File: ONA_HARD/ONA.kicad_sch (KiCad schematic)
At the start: 48 parts, among them J1 USB_C_Receptacle_USB2.0_16P, U1 ESP32-S3-WROOM-1U, U2 PC817, U3 LM2596S-5, U4 AMS1117-3.3, U6 MAX3485, U7 MAX3485, U8 MAX3485

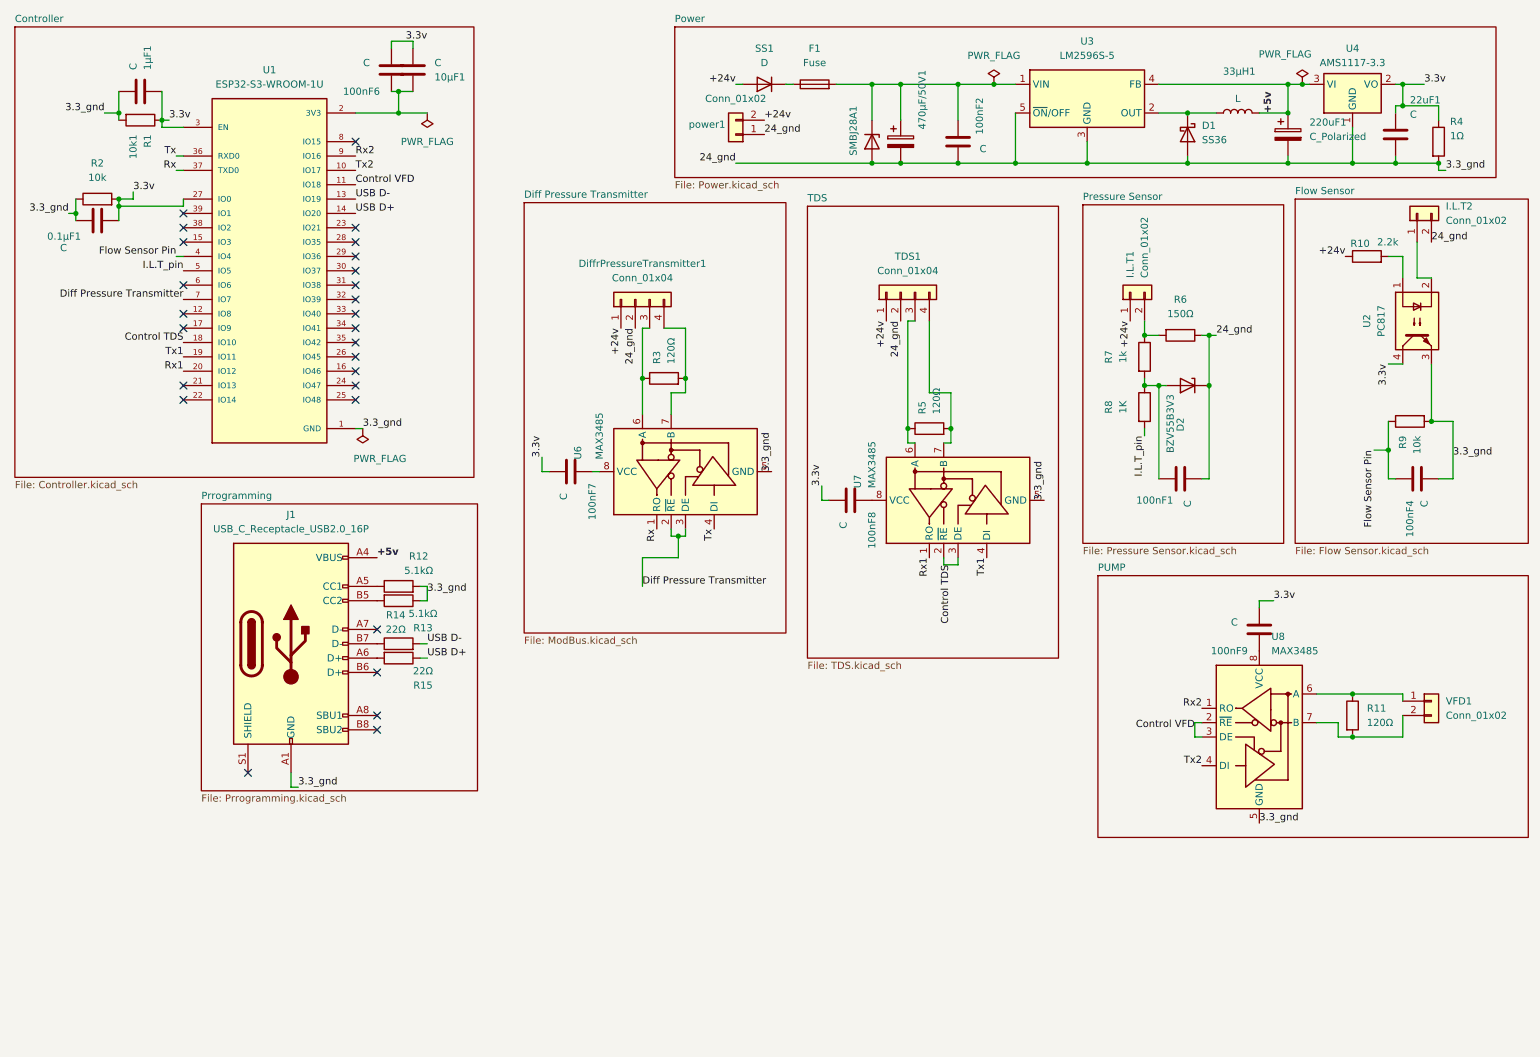
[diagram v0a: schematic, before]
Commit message: chore: remove .history folders and add to gitignore
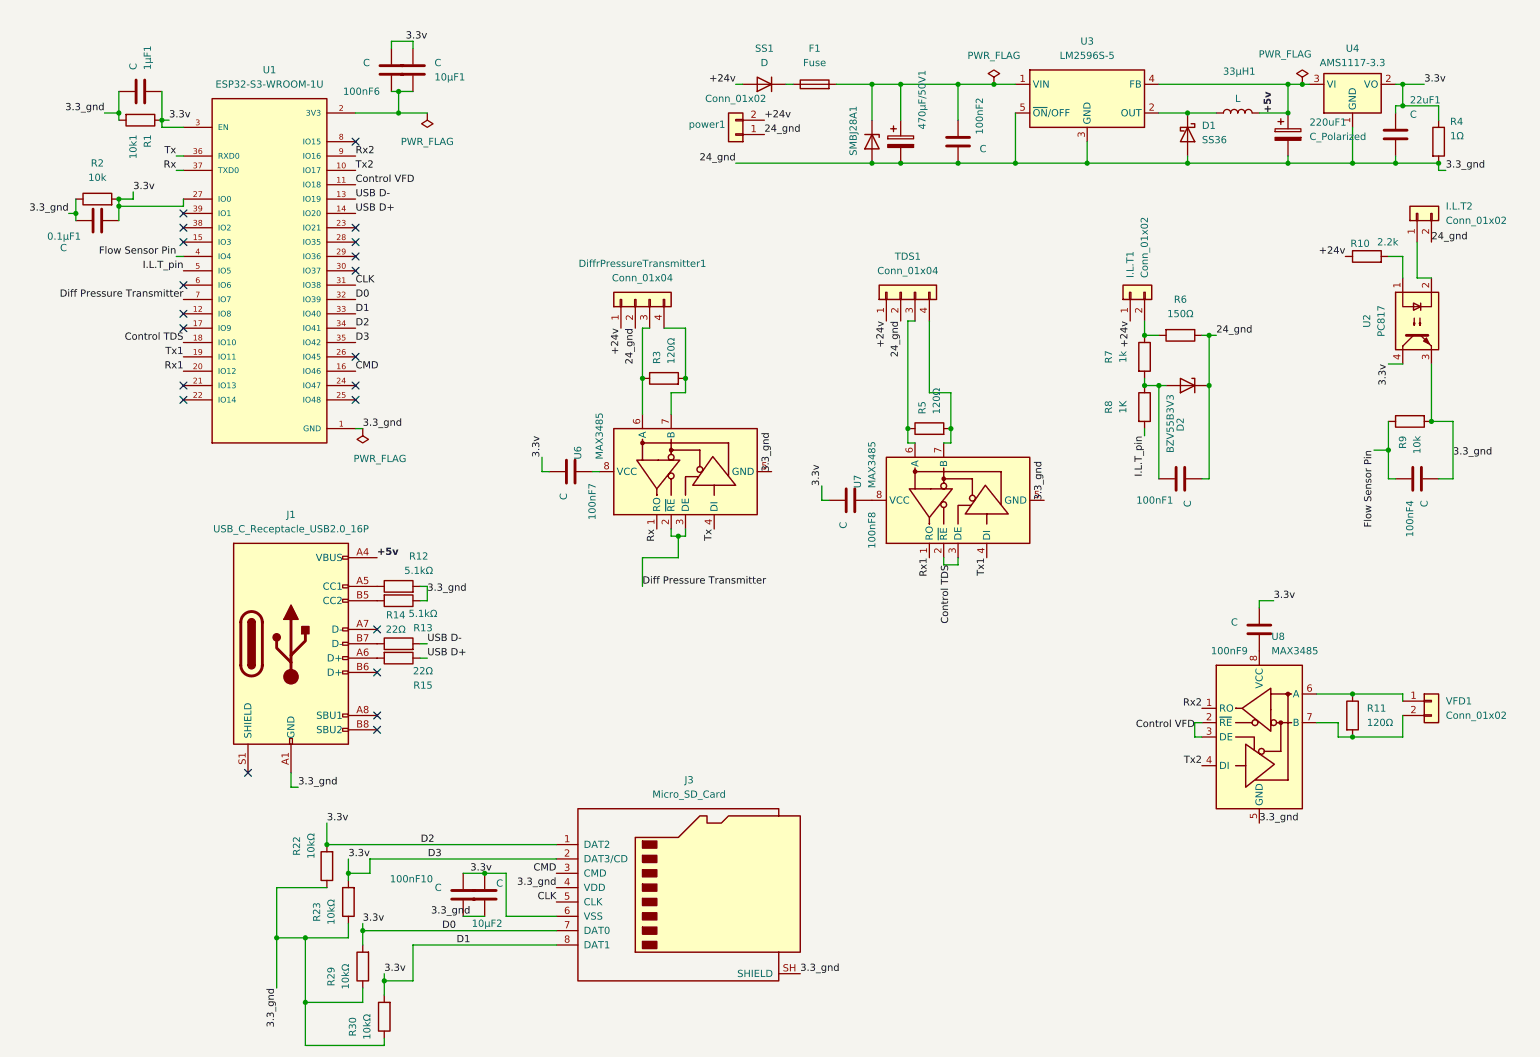
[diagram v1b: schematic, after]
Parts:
- added 100nF10, 10μF2: C, Capacitor_SMD:C_0805_2012Metric, symbol Device:C
- added J3: Micro_SD_Card, Connector_Card:microSD_HC_Hirose_DM3D-SF, symbol Connector:Micro_SD_Card
- added R22, R23, R29, R30: 10kΩ, Resistor_SMD:R_0805_2012Metric, symbol Device:R
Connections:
- net 3.3v: now also U1.32 (IO39), U1.33 (IO40), U1.34 (IO41), U1.35 (IO42), 100nF10.2, 10μF2.2, J3.1 (DAT2), J3.2 (DAT3/CD), J3.6 (VSS), J3.7 (DAT0), J3.8 (DAT1), R22.2, R23.2, R29.2, R30.2
- net GND: now also 100nF10.1, 10μF2.1, J3.4 (VDD), J3.SH (SHIELD), R22.1, R23.1, R29.1, R30.1
- net CMD: now reaches U1.16 (IO46)
- net CMD: now also J3.3 (CMD)
- net CLK: now reaches U1.31 (IO38)
- net CLK: now also J3.5 (CLK)
- no-connect marks 27 -> 21
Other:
- removed sheet Controller
- removed sheet Diff Pressure Transmitter
- removed sheet Flow Sensor
- removed sheet PUMP
- removed sheet Power
- removed sheet Pressure Sensor
- removed sheet Prrogramming
- removed sheet TDS
